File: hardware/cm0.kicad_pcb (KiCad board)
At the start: 4 copper layers, 53.2 x 36.4 mm, 12 parts, among them U1 H3, U2 H5TQ4G63EFR

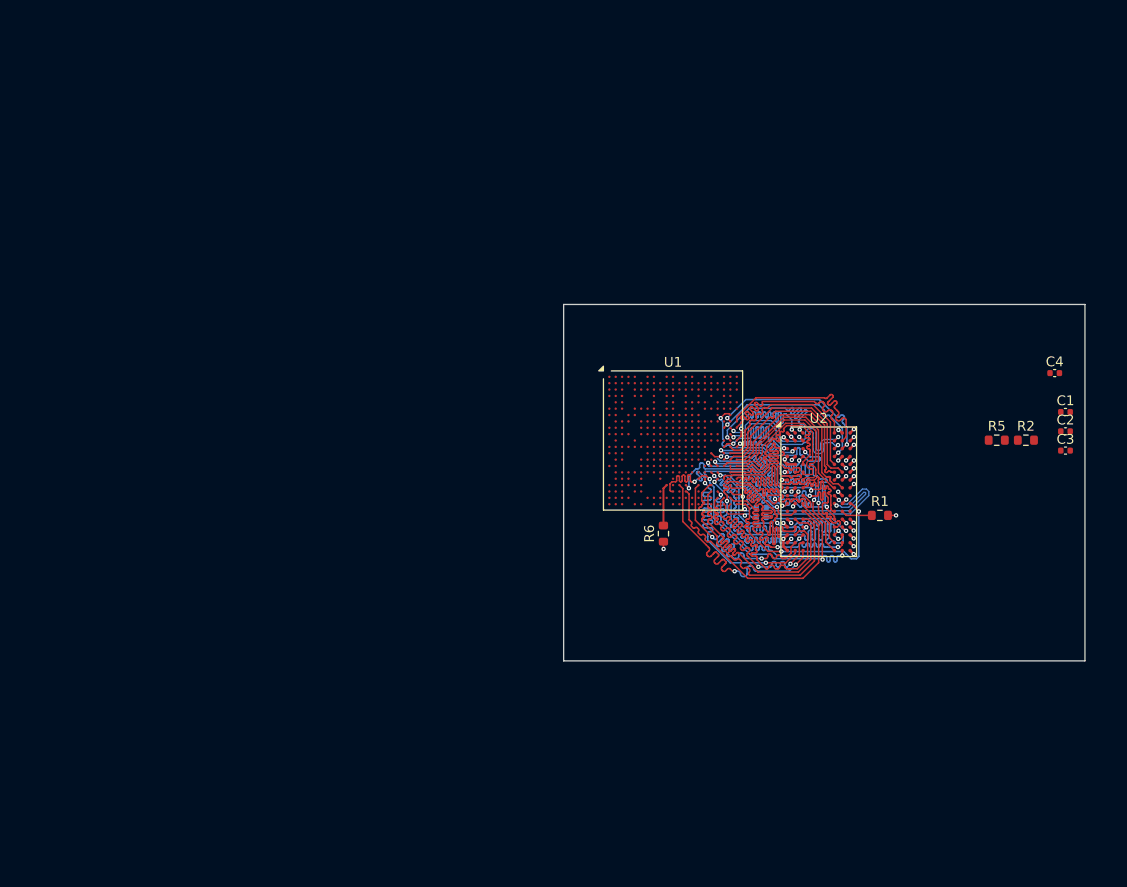
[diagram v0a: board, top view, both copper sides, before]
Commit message: Drew wifi, GPDI, and re-routed DDR3
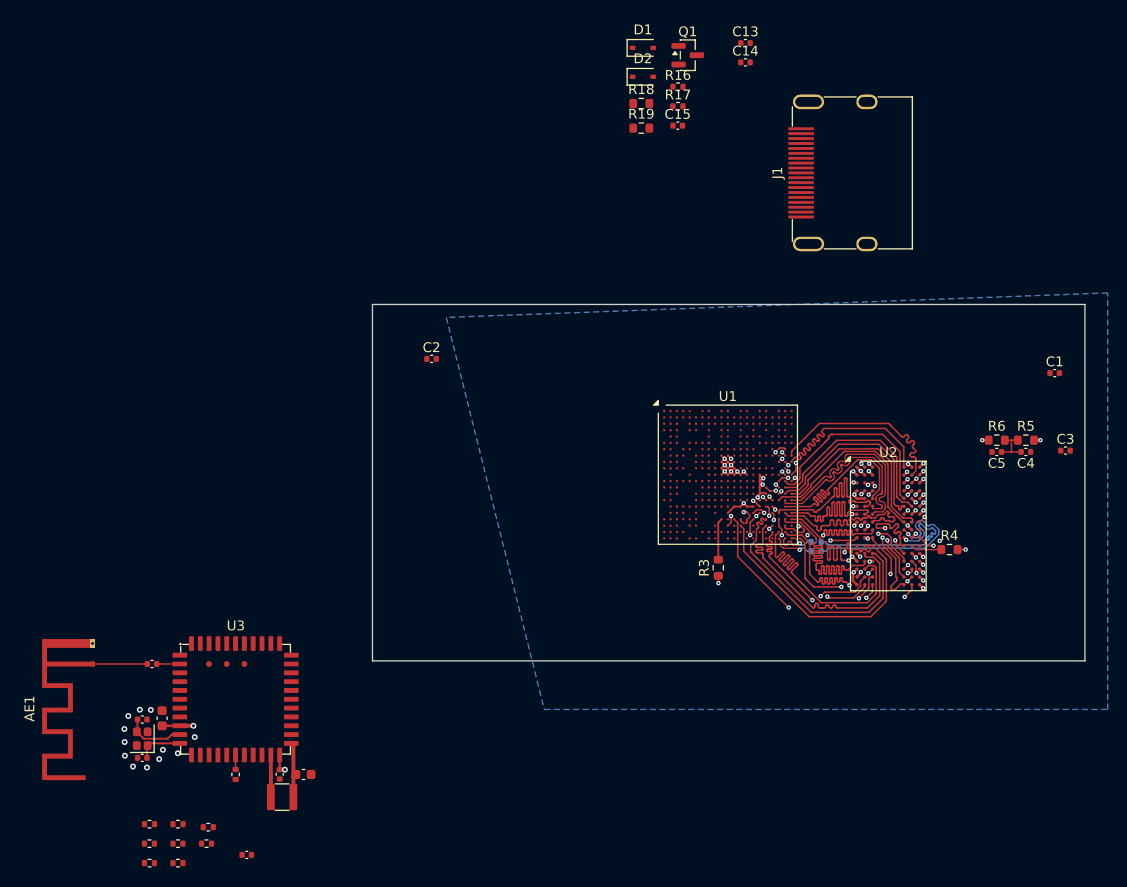
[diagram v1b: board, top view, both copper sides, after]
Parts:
- added AE1: Antenna_Shield, RF_Antenna:Texas_SWRA117D_2.4GHz_Left, F.Cu at (36.4, 127.9)
- added C10: 10pF, Capacitor_SMD:C_0402_1005Metric, F.Cu at (41.5, 137.4)
- added C11: 10pF, Capacitor_SMD:C_0402_1005Metric, F.Cu at (41.5, 133.5)
- added C12: 10uF, Capacitor_SMD:C_0603_1608Metric, F.Cu at (57.9, 139.1)
- added C13: 100nF, Capacitor_SMD:C_0402_1005Metric, F.Cu at (103.0, 64.5)
- added C14: 100nF, Capacitor_SMD:C_0402_1005Metric, F.Cu at (103.0, 66.5)
- added C15: 100nF, Capacitor_SMD:C_0402_1005Metric, F.Cu at (96.1, 72.9)
- added C2: 100nF, Capacitor_SMD:C_0402_1005Metric, F.Cu at (71.0, 96.7)
- added C6: 100nF, Capacitor_SMD:C_0402_1005Metric, F.Cu at (52.1, 147.3)
- added C7: 10uF, Capacitor_SMD:C_0603_1608Metric, F.Cu at (43.5, 133.4)
- added C8: 100nF, Capacitor_SMD:C_0402_1005Metric, F.Cu at (55.5, 139.1)
- added C9: 10pF, Capacitor_SMD:C_0402_1005Metric, F.Cu at (42.5, 127.9)
- added D1: 1N5819WS, Diode_SMD:D_SOD-323, F.Cu at (92.6, 65.0)
- added D2: 1N5819WS, Diode_SMD:D_SOD-323, F.Cu at (92.6, 67.9)
- added J1: GPDI_A, cm0:GPDI_A_XUNPU_001S, F.Cu at (112.1, 77.8)
- added L1: 4.7uH, cm0:L_SMD_3.0x3.0, F.Cu at (55.7, 141.4)
- added Q1: BSN20, Package_TO_SOT_SMD:SOT-23, F.Cu at (97.1, 65.7)
- added R10: 30k, Resistor_SMD:R_0402_1005Metric, F.Cu at (45.1, 148.2)
- added R11: 30k, Resistor_SMD:R_0402_1005Metric, F.Cu at (42.2, 148.2)
- added R12: 30k, Resistor_SMD:R_0402_1005Metric, F.Cu at (45.1, 144.2)
- added R13: 100k, Resistor_SMD:R_0402_1005Metric, F.Cu at (42.2, 144.2)
- added R14: 22, Resistor_SMD:R_0402_1005Metric, F.Cu at (51.0, 139.1)
- added R15: 100k, Resistor_SMD:R_0402_1005Metric, F.Cu at (42.2, 146.2)
- added R16: 30k, Resistor_SMD:R_0402_1005Metric, F.Cu at (96.1, 69.0)
- added R17: 30k, Resistor_SMD:R_0402_1005Metric, F.Cu at (96.1, 71.0)
- added R18: 2k, Resistor_SMD:R_0603_1608Metric, F.Cu at (92.4, 70.7)
- added R19: 2k, Resistor_SMD:R_0603_1608Metric, F.Cu at (92.4, 73.2)
- added R7: 10k, Resistor_SMD:R_0402_1005Metric, F.Cu at (48.0, 146.2)
- added R8: 30k, Resistor_SMD:R_0402_1005Metric, F.Cu at (48.2, 144.5)
- added R9: 30k, Resistor_SMD:R_0402_1005Metric, F.Cu at (45.1, 146.2)
- added U3: AP6212, cm0:AP6212, F.Cu at (51.0, 131.5)
- added Y1: 26MHz, Crystal:Crystal_SMD_2016-4Pin_2.0x1.6mm, F.Cu at (41.5, 135.5)
- moved R4 7.91 mm to (123.8, 116.2)
- moved U2 7.91 mm to (117.6, 113.8)
- moved C5 7.32 mm to (128.7, 106.2), turned to 180 degrees
- moved R1 6.60 mm to (110.2, 116.4)
- moved R2 6.60 mm to (110.2, 115.4)
- moved R3 6.60 mm to (100.3, 118.0)
- moved U1 6.60 mm to (101.2, 108.5)
- moved C4 5.74 mm to (131.7, 106.2), turned to 180 degrees
- renumbered C4 to C1, C1 to C4, C2 to C5, R3 to R1, R4 to R2, R6 to R3, R1 to R4, R2 to R5, R5 to R6
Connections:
- U1 pad A21: (no net) -> GND
- U1 pad A5: (no net) -> /H3/USB_D0+
- U1 pad A7: (no net) -> /H3/USB_D2+
- U1 pad A8: (no net) -> /H3/USB_D2-
- U1 pad AA1: (no net) -> GND
- U1 pad B1: (no net) -> unconnected-(U1C-PG13-PadB1)
- U1 pad B5: (no net) -> /H3/USB_D0-
- U1 pad B6: (no net) -> /H3/USB_D1+
- U1 pad B7: (no net) -> /H3/USB_D1-
- U1 pad B8: (no net) -> /H3/USB_D3+
- U1 pad B9: (no net) -> /H3/USB_D3-
- U1 pad C1: (no net) -> /H3/SDIO_D3
- U1 pad C2: (no net) -> /H3/SDIO_D2
- U1 pad C3: (no net) -> /H3/~{BT_RTS}
- U1 pad D1: (no net) -> unconnected-(U1C-PG12-PadD1)
- U1 pad D2: (no net) -> unconnected-(U1C-PG11-PadD2)
- U1 pad D3: (no net) -> /H3/BT_RXD
- U1 pad E2: (no net) -> /GPDI/GPDI_CLK-
- U1 pad E3: (no net) -> /H3/~{BT_CTS}
- U1 pad F1: (no net) -> /GPDI/GPDI_D0-
- U1 pad F2: (no net) -> /GPDI/GPDI_CLK+
- U1 pad F3: (no net) -> /H3/SDIO_D1
- U1 pad G1: (no net) -> /GPDI/GPDI_D0+
- U1 pad G10: (no net) -> unconnected-(U1B-VDD-EFUSE-PadG10)
- U1 pad G11: (no net) -> +3V3
- U1 pad G2: (no net) -> /GPDI/GPDI_D1-
- U1 pad G4: (no net) -> /H3/BT_TXD
- U1 pad G5: (no net) -> /GPDI/GPDI_CEC
- U1 pad G8: (no net) -> GND
- U1 pad H10: (no net) -> VDD-SYS
- U1 pad H11: (no net) -> unconnected-(U1B-VDD-EFUSEEBP-PadH11)
- U1 pad H12: (no net) -> GND
- U1 pad H15: (no net) -> GND
- U1 pad H2: (no net) -> /GPDI/GPDI_D1+
- U1 pad H3: (no net) -> /GPDI/GPDI_SDA
- U1 pad H4: (no net) -> /H3/SDIO_D0
- U1 pad H7: (no net) -> +3V3
- U1 pad J1: (no net) -> /GPDI/GPDI_D2+
- U1 pad J10: (no net) -> VDD-SYS
- U1 pad J11: (no net) -> VDD-SYS
- U1 pad J12: (no net) -> VDD-SYS
- U1 pad J13: (no net) -> GND
- U1 pad J16: (no net) -> GND
- U1 pad J2: (no net) -> /GPDI/GPDI_D2-
- U1 pad J3: (no net) -> /H3/SDIO_CLK
- U1 pad J6: (no net) -> +3V3
- U1 pad J7: (no net) -> VDD-CPUS
- U1 pad J8: (no net) -> VDD-CPUS
- U1 pad J9: (no net) -> GND
- U1 pad K10: (no net) -> VDD-SYS
- U1 pad K11: (no net) -> VDD-SYS
- U1 pad K12: (no net) -> VDD-SYS
- U1 pad K13: (no net) -> GND
- U1 pad K14: (no net) -> GND
- U1 pad K15: (no net) -> GND
- U1 pad K16: (no net) -> GND
- U1 pad K3: (no net) -> /GPDI/GPDI_SDA
- U1 pad K7: (no net) -> GND
- U1 pad K8: (no net) -> GND
- U1 pad K9: (no net) -> GND
- U1 pad L10: (no net) -> VDD-SYS
- U1 pad L11: (no net) -> VDD-SYS
- U1 pad L12: (no net) -> VDD-SYS
- U1 pad L13: (no net) -> VDD-SYS
- U1 pad L14: (no net) -> VDD-SYS
- U1 pad L15: (no net) -> GND
- U1 pad L16: (no net) -> +1V5
- U1 pad L2: (no net) -> /H3/SDIO_CMD
- U1 pad L8: (no net) -> GND
- U1 pad L9: (no net) -> GND
- U1 pad M10: (no net) -> GND
- U1 pad M11: (no net) -> GND
- U1 pad M12: (no net) -> GND
- U1 pad M13: (no net) -> GND
- U1 pad M14: (no net) -> GND
- U1 pad M15: (no net) -> GND
- U1 pad M16: (no net) -> +1V5
- U1 pad M2: (no net) -> /GPDI/GPDI_HPD
- U1 pad M3: (no net) -> unconnected-(U1C-PG10-PadM3)
- U1 pad M5: (no net) -> GND
- U1 pad M7: (no net) -> GND
- U1 pad M8: (no net) -> GND
- U1 pad M9: (no net) -> GND
- U1 pad N10: (no net) -> GND
- U1 pad N11: (no net) -> GND
- U1 pad N12: (no net) -> GND
- U1 pad N13: (no net) -> GND
- U1 pad N14: (no net) -> GND
- U1 pad N15: (no net) -> GND
- U1 pad N16: (no net) -> +1V5
- U1 pad N7: (no net) -> GND
- U1 pad N8: (no net) -> VDD-CPUX
- U1 pad N9: (no net) -> GND
- U1 pad P10: (no net) -> GND
- U1 pad P11: (no net) -> GND
- U1 pad P12: (no net) -> GND
- U1 pad P13: (no net) -> GND
- U1 pad P14: (no net) -> GND
- U1 pad P15: (no net) -> GND
- U1 pad P16: (no net) -> +1V5
- U1 pad P17: (no net) -> +1V5
- U1 pad P6: (no net) -> VDD-CPUX
- U1 pad P7: (no net) -> VDD-CPUX
- U1 pad P8: (no net) -> VDD-CPUX
- U1 pad P9: (no net) -> VDD-CPUX
- U1 pad R10: (no net) -> GND
- U1 pad R11: (no net) -> GND
- U1 pad R12: (no net) -> GND
- U1 pad R13: (no net) -> GND
- U1 pad R14: (no net) -> GND
- U1 pad R16: (no net) -> +1V5
- U1 pad R6: (no net) -> VDD-CPUX
- U1 pad R7: (no net) -> VDD-CPUX
- U1 pad R8: (no net) -> VDD-CPUX
- U1 pad R9: (no net) -> GND
- U1 pad T11: (no net) -> GND
- U1 pad T12: (no net) -> +1V5
- U1 pad T13: (no net) -> +1V5
- U1 pad T14: (no net) -> +1V5
- U1 pad T15: (no net) -> +1V5
- U1 pad T6: (no net) -> VDD-CPUX
- U1 pad T7: (no net) -> VDD-CPUX
- U1 pad T8: (no net) -> VDD-CPUX
- U1 pad U11: (no net) -> +1V5
- U1 pad U6: (no net) -> VDD-CPUX
- U1 pad U9: (no net) -> VDD-CPUX
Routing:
- net VDD-SYS: track 0.00 -> 11.0 mm, vias 0 -> 7
- net VREF: track 9.34 -> 19.8 mm, vias 2 -> 3
- net +1V5: track 9.79 -> 19.7 mm, vias 17 -> 22
- net /DDR3/DQ13: track 17.8 -> 10.8 mm
- net Net-(U3-XTAL_IN): track 0.00 -> 6.14 mm
- net /DDR3/BA1: track 18.1 -> 24.1 mm
- net Net-(U3-VIN_LDO): track 0.00 -> 5.82 mm
- net Net-(AE1-A): track 0.00 -> 5.59 mm
- net +3V3: track 0.00 -> 4.95 mm, vias 0 -> 2
- net /DDR3/DQ15: track 17.8 -> 12.9 mm
- net Net-(U3-XTAL_OUT): track 0.00 -> 4.76 mm
- net Net-(U3-VIN_LDO_OUT): track 0.00 -> 4.55 mm
- net /DDR3/CLK-: track 15.1 -> 19.6 mm
- net /DDR3/CLK+: track 16.4 -> 19.6 mm
- net /DDR3/A4: track 21.4 -> 24.2 mm
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- added copper zone on B.Cu, net +1V5
- added copper zone on In1.Cu, net GND
- added copper zone on In2.Cu, net GND
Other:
- board size 53.2 x 36.4 mm -> 72.7 x 36.4 mm
